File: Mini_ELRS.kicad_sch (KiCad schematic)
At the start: 24 parts, among them J1 Conn_01x06, J2 Conn_01x06, J3 Conn_01x06, SW1 SW_Push, U1 ESP32-PICO-D4, U2 TC2014-3.3VxCTTR, U3 SX1280IMLTRT, Y1 Crystal_GND24_Small

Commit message: stash for esp8266
Signed-off-by: ncerzzk <huangzzk@bupt.edu.cn>
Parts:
- removed D2: LED, LED_SMD:LED_0603_1608Metric, symbol Device:LED
- removed J1, J2: Conn_01x06, Connector_PinHeader_2.54mm:PinHeader_1x06_P2.54mm_Vertical, symbol Connector_Generic:Conn_01x06
- removed U1: ESP32-PICO-D4, Package_DFN_QFN:QFN-48-1EP_7x7mm_P0.5mm_EP5.3x5.3mm, symbol RF_Module:ESP32-PICO-D4
- added AE2: Antenna, RF_Antenna:Texas_SWRA117D_2.4GHz_Left, symbol Device:Antenna
- added C10: 0.1uF, Capacitor_SMD:C_0402_1005Metric, symbol Device:C
- added R4: NC, Resistor_SMD:R_0402_1005Metric, symbol Device:R
- added R5: 10K, Resistor_SMD:R_0402_1005Metric, symbol Device:R
- added U1: ESP8266EX, Package_DFN_QFN:QFN-32-1EP_5x5mm_P0.5mm_EP3.45x3.45mm, symbol MCU_Espressif:ESP8266EX
- C1, C2, C3, C4, C5, C6, C7, C8, C9: footprint Capacitor_SMD:C_0603_1608Metric -> Capacitor_SMD:C_0402_1005Metric
- R1, R2: footprint Resistor_SMD:R_0603_1608Metric -> Resistor_SMD:R_0402_1005Metric
- R3: value 10K -> 12K; footprint Resistor_SMD:R_0603_1608Metric -> Resistor_SMD:R_0402_1005Metric
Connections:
- net +3V3: now also U1.1 (VDDA), U1.11 (VDDPST), U1.17 (VDDPST), U1.29 (VDDD), U1.3 (VDD3P3), U1.30 (VDDA), U1.4 (VDD3P3)
- net BUSY: now also U1.24 (GPIO5)
- net DIO1: now also R4.2
- net GND: now also R3.1, C10.1, R5.2, U1.33 (GND)
- net MISO: now also U1.10 (MTDI)
- net MOSI: now also U1.12 (MTCK)
- net NRST: now also U1.16 (GPIO4)
- net NSS: now also R5.1, U1.13 (MTDO)
- net RX: now also U1.25 (U0RXD)
- net SCK: now also U1.9 (MTMS)
- net TX: now also U1.26 (U0TXD)
- net at C1.1, R1.2: now also U1.7 (CHIP_PU)
- net at SW1.1: now also U1.15 (GPIO0)
- net LED: no longer names the net of R3.2
- net LED: now also U1.31 (RES12K)
- new net: AE2.1 (A), U1.2 (LNA)
- new net: R4.1, U1.14 (GPIO2)
- new net: C10.2, U1.5 (VDD_RTC)
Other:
- moved on the sheet: C1, D1, J3, R1, R2, SW1

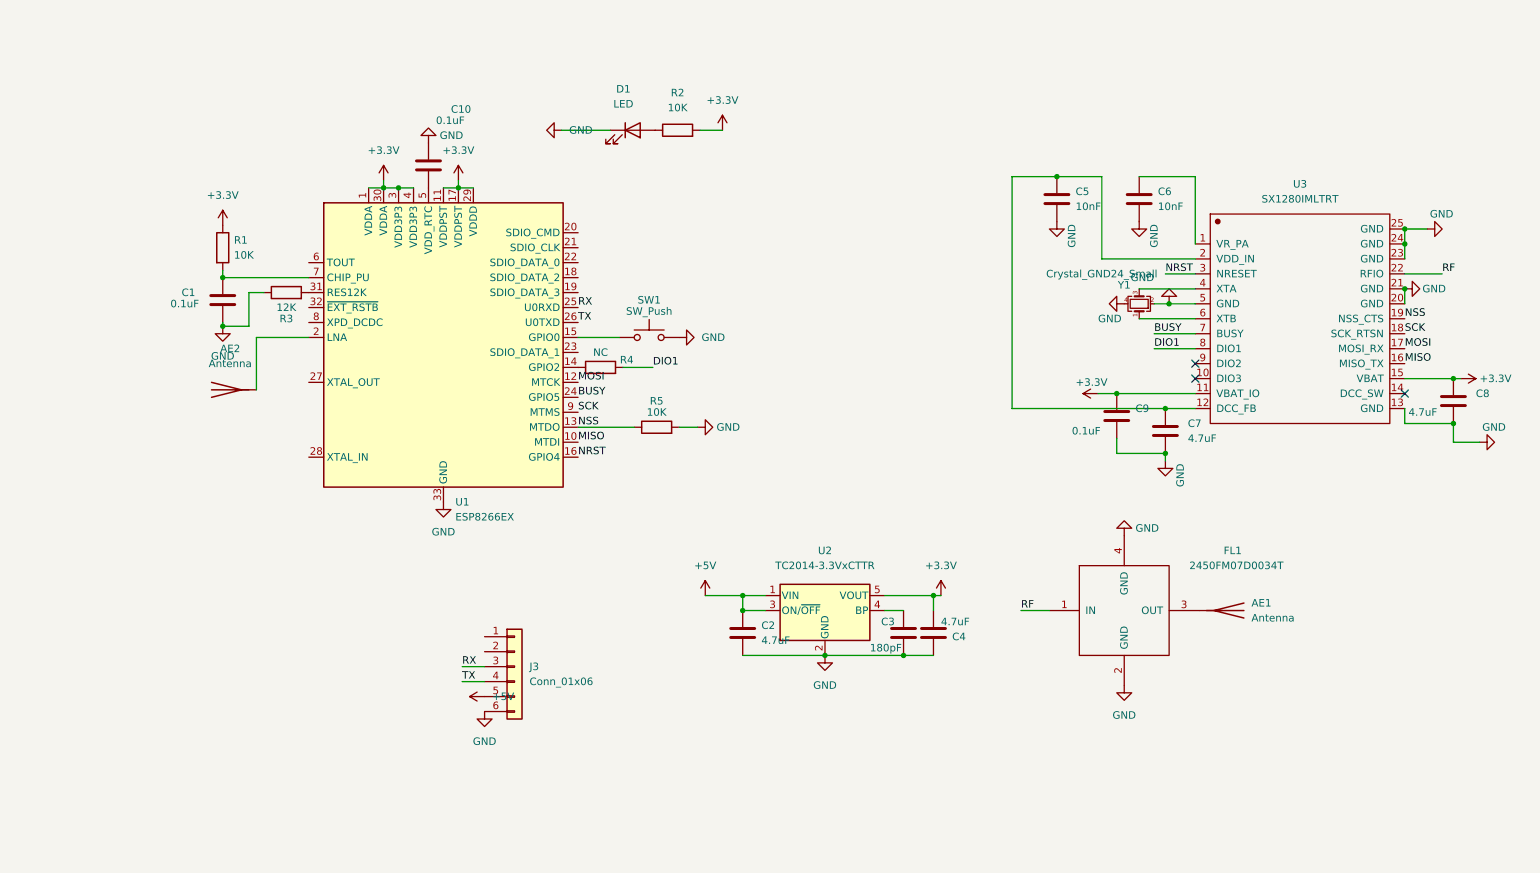
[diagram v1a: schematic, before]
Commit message: update esp8266 v0.7
Signed-off-by: ncerzzk <huangzzk@bupt.edu.cn>
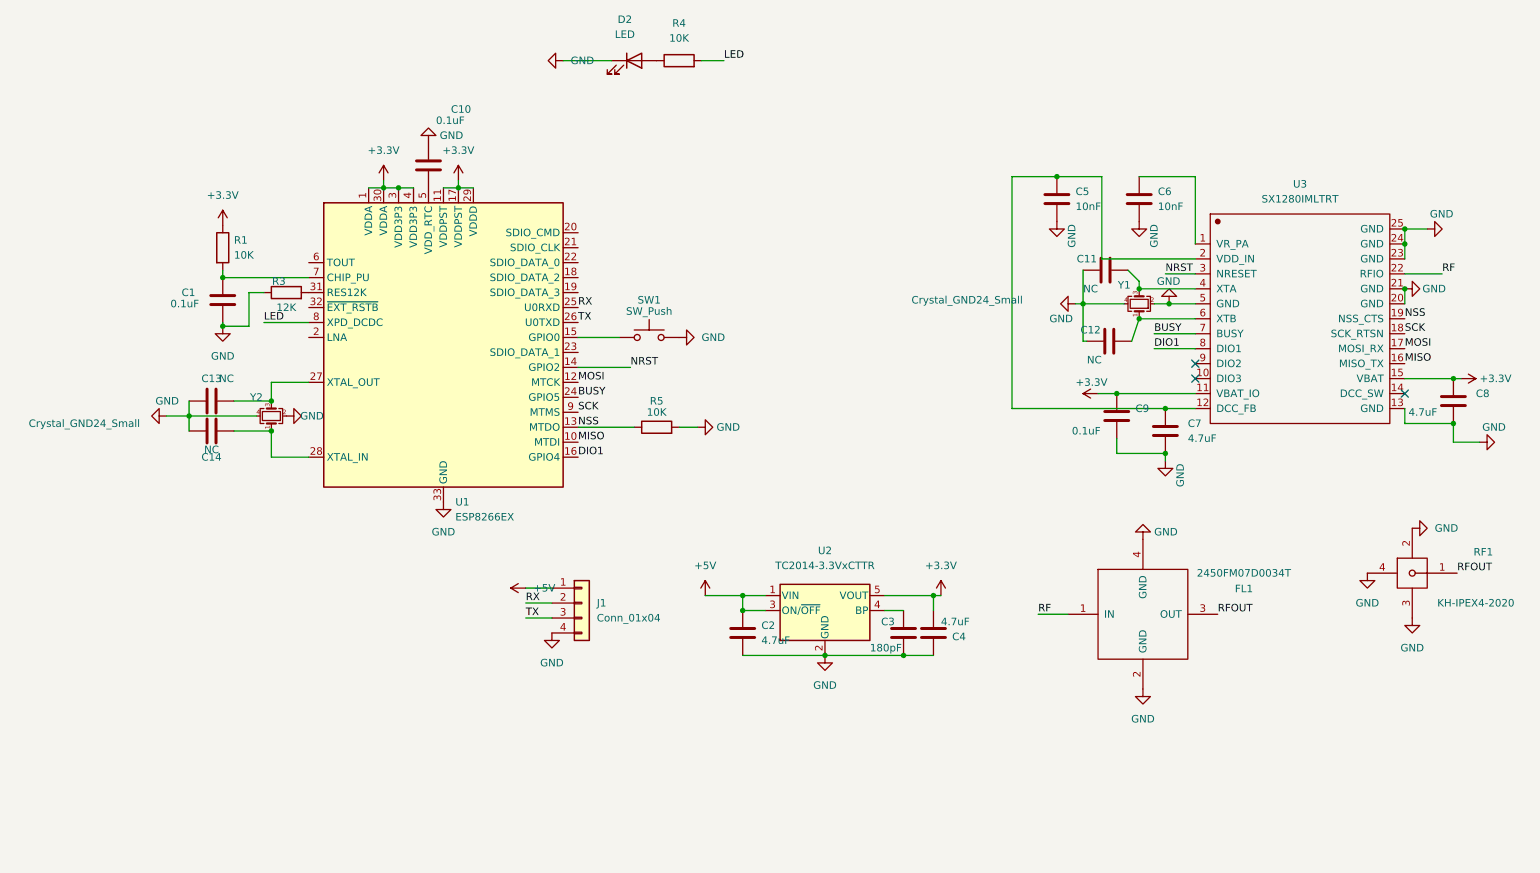
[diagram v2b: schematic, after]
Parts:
- removed AE1: Antenna, RF_Antenna:Johanson_2450AT43F0100, symbol Device:Antenna
- removed AE2: Antenna, RF_Antenna:Texas_SWRA117D_2.4GHz_Left, symbol Device:Antenna
- removed D1: LED, LED_SMD:LED_0603_1608Metric, symbol Device:LED
- removed J3: Conn_01x06, Connector_PinHeader_2.54mm:PinHeader_1x06_P2.54mm_Vertical, symbol Connector_Generic:Conn_01x06
- removed R2: 10K, Resistor_SMD:R_0402_1005Metric, symbol Device:R
- added C11, C12, C13, C14: NC, Capacitor_SMD:C_0402_1005Metric, symbol Device:C
- added D2: LED, LED_SMD:LED_0603_1608Metric, symbol Device:LED
- added J1: Conn_01x04, Connector_PinHeader_2.54mm:PinHeader_1x04_P2.54mm_Vertical, symbol Connector_Generic:Conn_01x04
- added RF1: KH-IPEX4-2020, kicad_lceda:IPEX4-SMD_4P-L1.8-W1.7-LS2.0-L_KH-IPEX4-2020, symbol ic:KH-IPEX4-2020
- added Y2: Crystal_GND24_Small, Crystal:Crystal_SMD_2520-4Pin_2.5x2.0mm, symbol Device:Crystal_GND24_Small
- R4: value NC -> 10K
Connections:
- net +5V: now also J1.1 (Pin_1)
- net DIO1: now also U1.16 (GPIO4); no longer R4.2
- net GND: now also C11.1, C12.1, C13.1, C14.1, D2.1 (K), J1.4 (Pin_4), RF1.2, RF1.3, RF1.4, Y2.2, Y2.4
- net NRST: now also U1.14 (GPIO2); no longer U1.16 (GPIO4)
- net RX: now also J1.2 (Pin_2)
- net TX: now also J1.3 (Pin_3)
- net at R4.1: now also D2.2 (A); no longer U1.14 (GPIO2)
- net at U1.27 (XTAL_OUT): now also C13.2, Y2.3
- net at U1.28 (XTAL_IN): now also C14.2, Y2.1
- net LED: now reaches U1.8 (XPD_DCDC)
- net LED: now also R4.2
- net RFOUT: now reaches FL1.3 (OUT)
- net RFOUT: now also RF1.1
- net at U3.6 (XTB), Y1.1: now also C12.2
- net at U3.4 (XTA), Y1.3: now also C11.2

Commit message: update
Signed-off-by: huangzzk <huangcmzzk@gmail.com>
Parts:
- Y1, Y2: value Crystal_GND24_Small -> 52M
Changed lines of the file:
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@@
     (in_bom yes) (on_board yes)
     (property "Reference" "Y2" (id 0) (at 34.925 88.265 90))
-    (property "Value" "Crystal_GND24_Small" (id 1) (at 5.715 92.71 90))
+    (property "Value" "52M" (id 1) (at 33.655 92.71 90))
     (property "Footprint" "Crystal:Crystal_SMD_2520-4Pin_2.5x2.0mm" (id 2) (at 37.465 91.44 0)
       (effects (font (size 1.27 1.27)) hide)
@@
     (in_bom yes) (on_board yes)
     (property "Reference" "Y1" (id 0) (at 182.245 69.215 90))
-    (property "Value" "Crystal_GND24_Small" (id 1) (at 155.575 71.755 90))
+    (property "Value" "52M" (id 1) (at 180.975 74.295 90))
     (property "Footprint" "Crystal:Crystal_SMD_2520-4Pin_2.5x2.0mm" (id 2) (at 184.785 72.39 0)
       (effects (font (size 1.27 1.27)) hide)
@@
     )
     (path "/b2837d6b-6cc1-45c4-aa75-fd2bb220208e"
-      (reference "Y1") (unit 1) (value "Crystal_GND24_Small") (footprint "Crystal:Crystal_SMD_2520-4Pin_2.5x2.0mm")
+      (reference "Y1") (unit 1) (value "52M") (footprint "Crystal:Crystal_SMD_2520-4Pin_2.5x2.0mm")
     )
     (path "/6ceec7ee-4bcd-4970-abb4-553246f38eb5"
-      (reference "Y2") (unit 1) (value "Crystal_GND24_Small") (footprint "Crystal:Crystal_SMD_2520-4Pin_2.5x2.0mm")
-    )
-  )
+      (reference "Y2") (unit 1) (value "52M") (footprint "Crystal:Crystal_SMD_2520-4Pin_2.5x2.0mm")
+    )
+  )

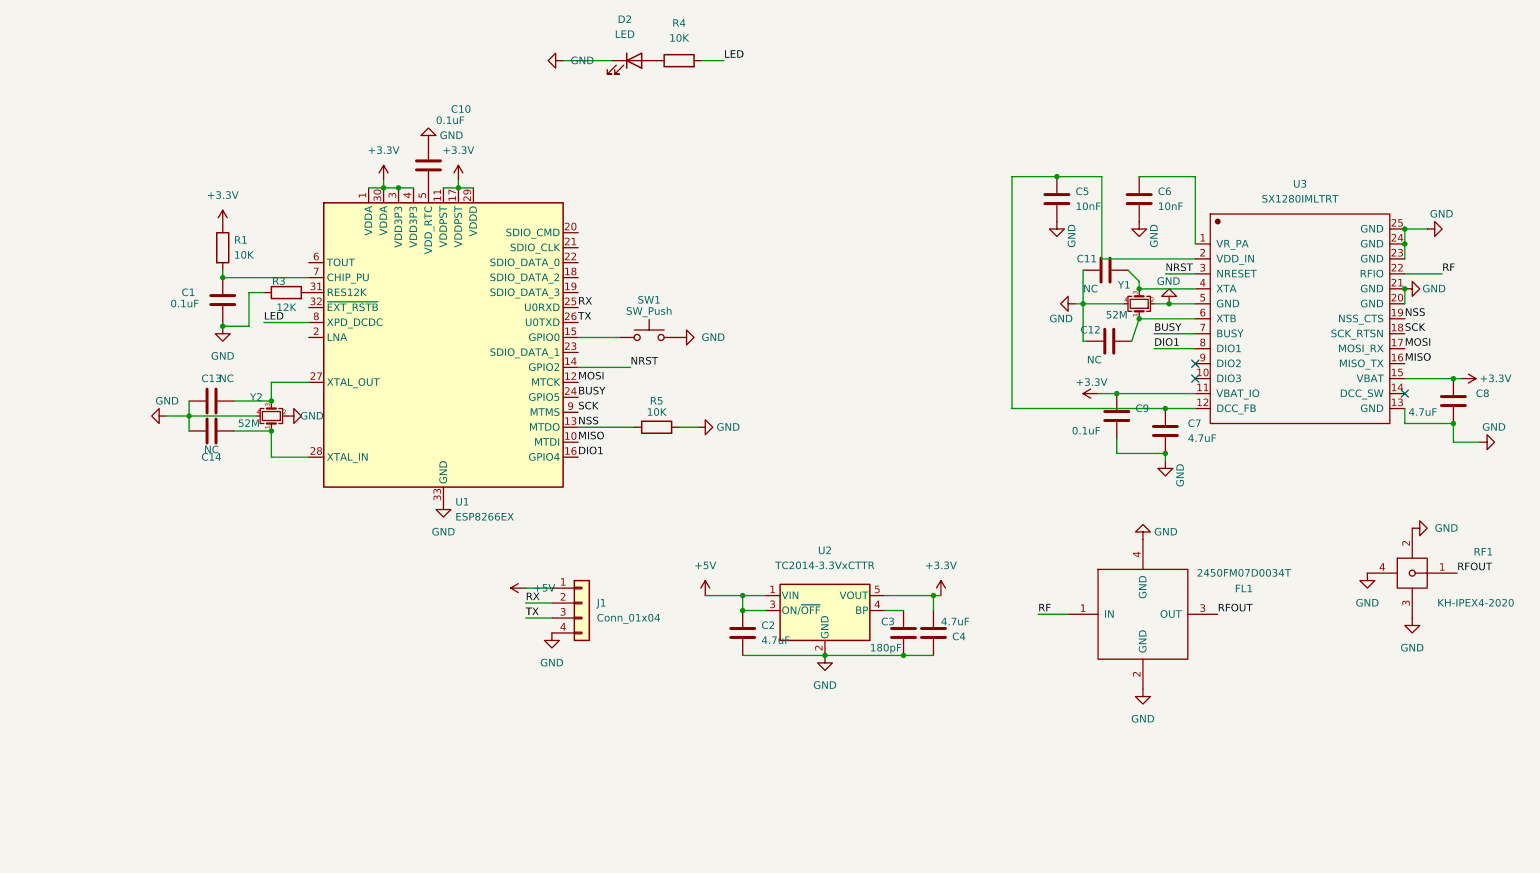
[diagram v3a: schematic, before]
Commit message: remove some unnecessary cap/res, remove ipex4.0 , add esp8266 lna
Signed-off-by: huangzzk <huangcmzzk@gmail.com>
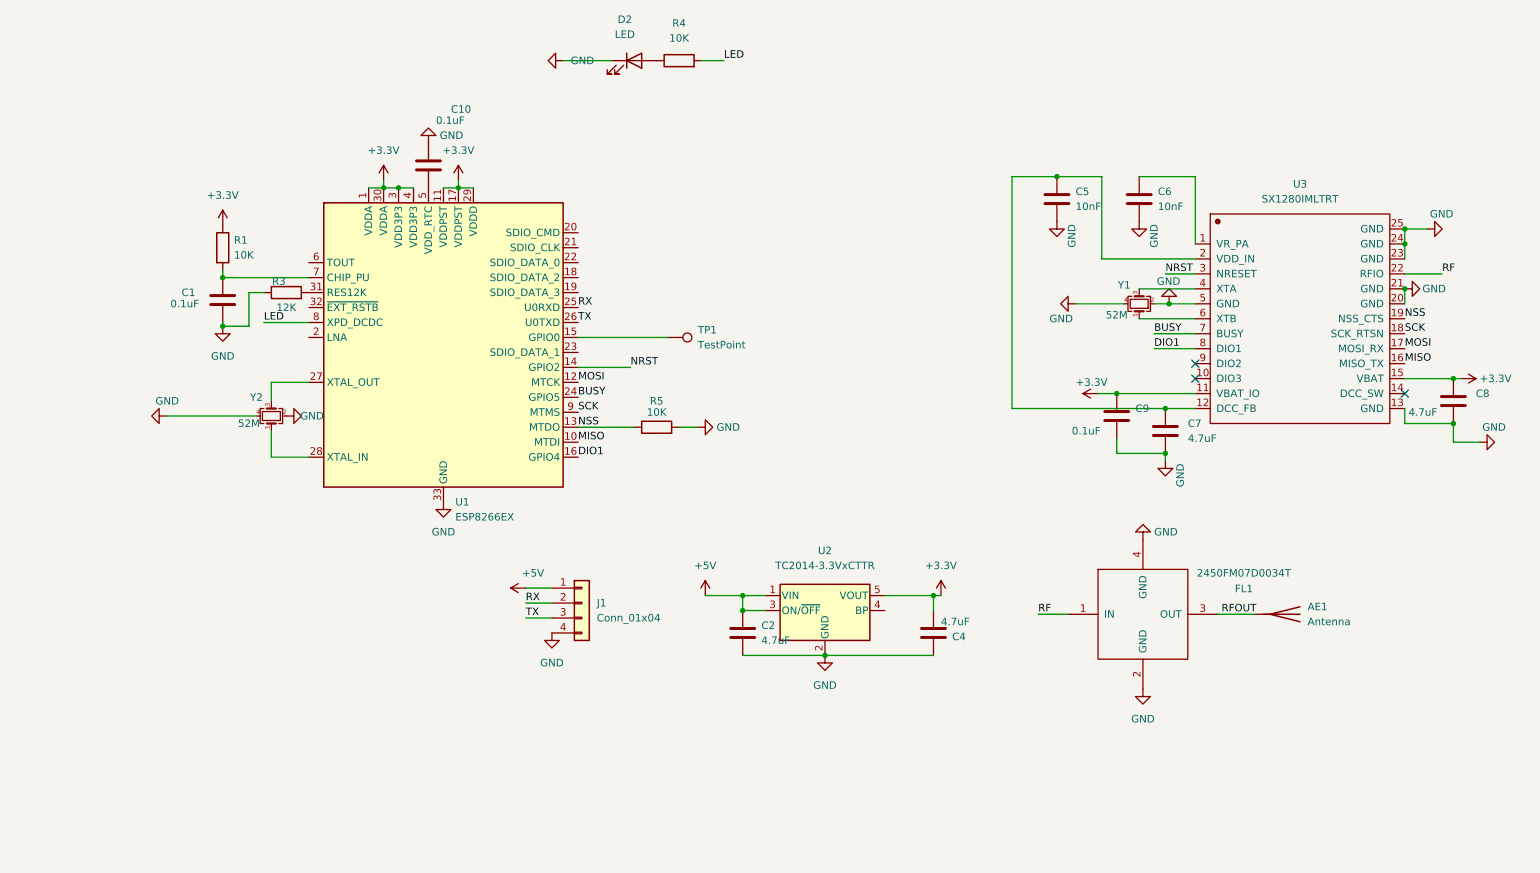
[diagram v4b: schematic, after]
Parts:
- removed C11, C12, C13, C14: NC, Capacitor_SMD:C_0402_1005Metric, symbol Device:C
- removed C3: 180pF, Capacitor_SMD:C_0402_1005Metric, symbol Device:C
- removed RF1: KH-IPEX4-2020, kicad_lceda:IPEX4-SMD_4P-L1.8-W1.7-LS2.0-L_KH-IPEX4-2020, symbol ic:KH-IPEX4-2020
- removed SW1: SW_Push, Button_Switch_SMD:SW_Push_SPST_NO_Alps_SKRK, symbol Switch:SW_Push
- added AE1: Antenna, RF_Antenna:Johanson_2450AT43F0100, symbol Device:Antenna
- added TP1: TestPoint, TestPoint:TestPoint_Pad_1.0x1.0mm, symbol Connector:TestPoint
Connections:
- net RFOUT: now also AE1.1 (A)
- net at U1.15 (GPIO0): now also TP1.1
